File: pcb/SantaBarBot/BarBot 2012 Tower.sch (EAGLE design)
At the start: 42 parts, among them J1 AVR_SPI_PRG_62X3_LOCK, U1 ATMEGA328P, U2 L298_BRIDGE_DRIVER, U3 742G04DBVR, U5 LMV324IDR, U6 SN75HVD179D, U7 742G04DBVR, U8 SN75HVD179D, U9 LMV324IDR

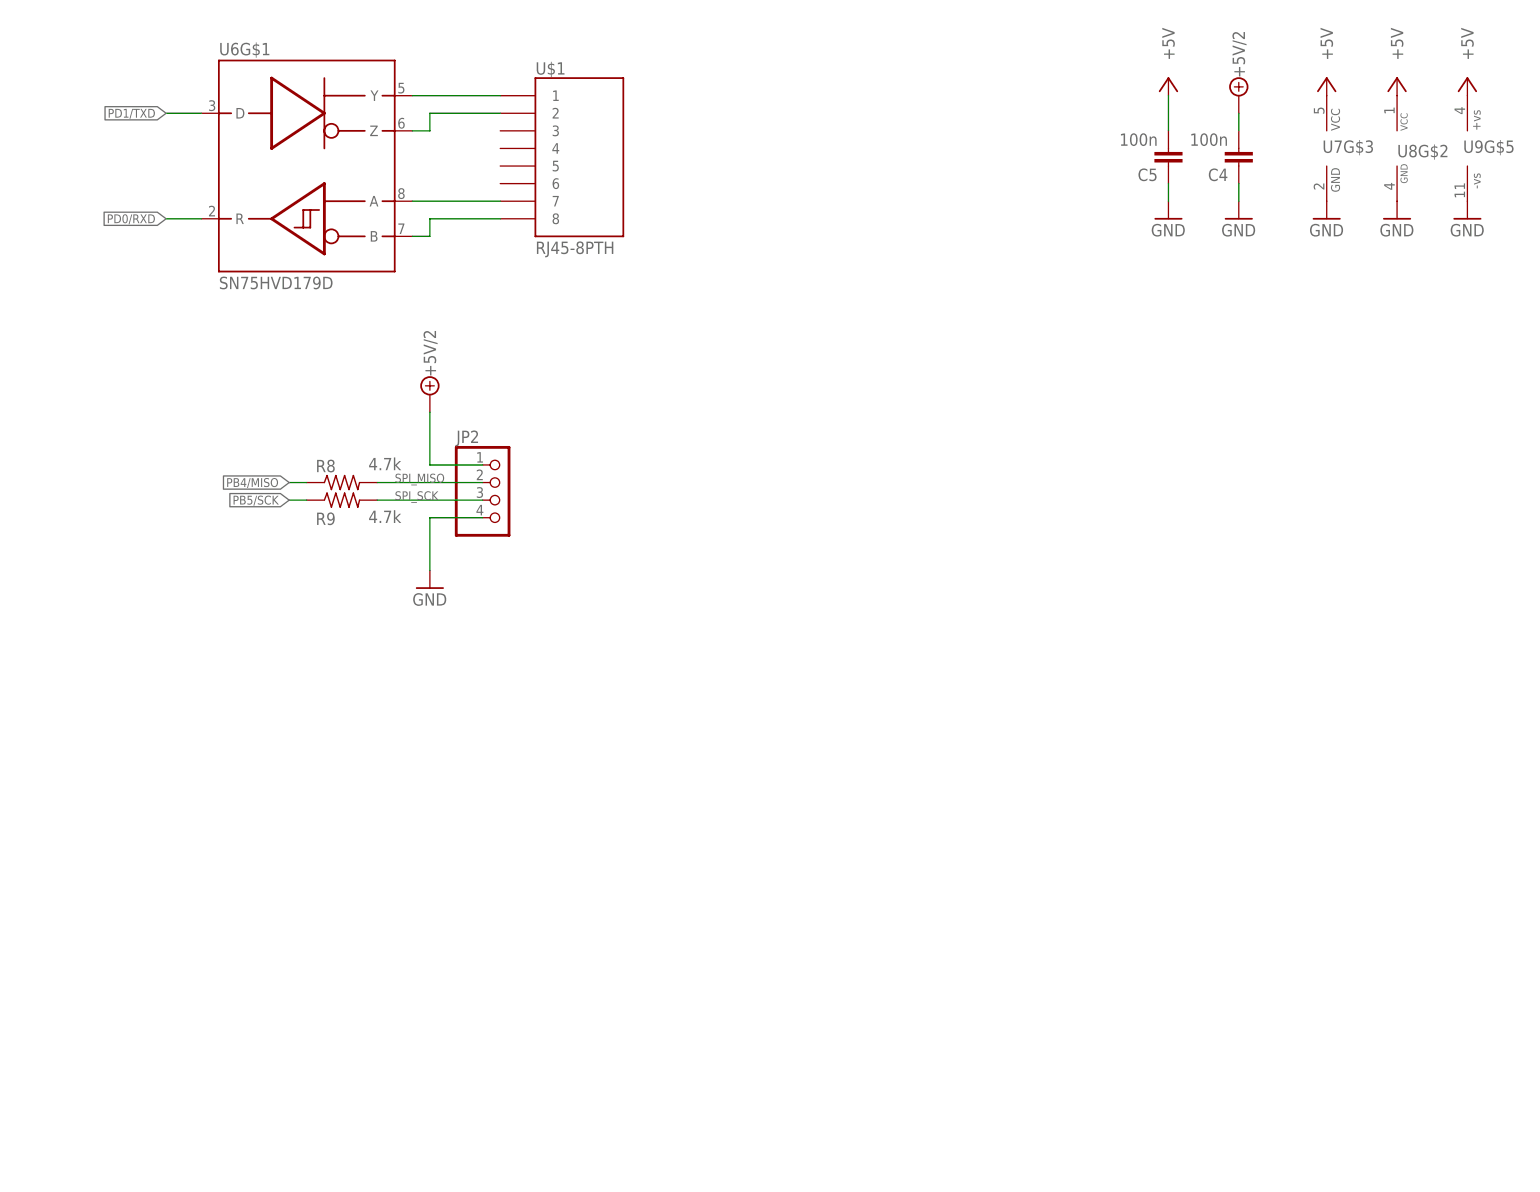
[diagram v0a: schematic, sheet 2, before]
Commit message: Started PCB layout, cleaning up schematic.  Added RS485 termination, fixed duplicate chips
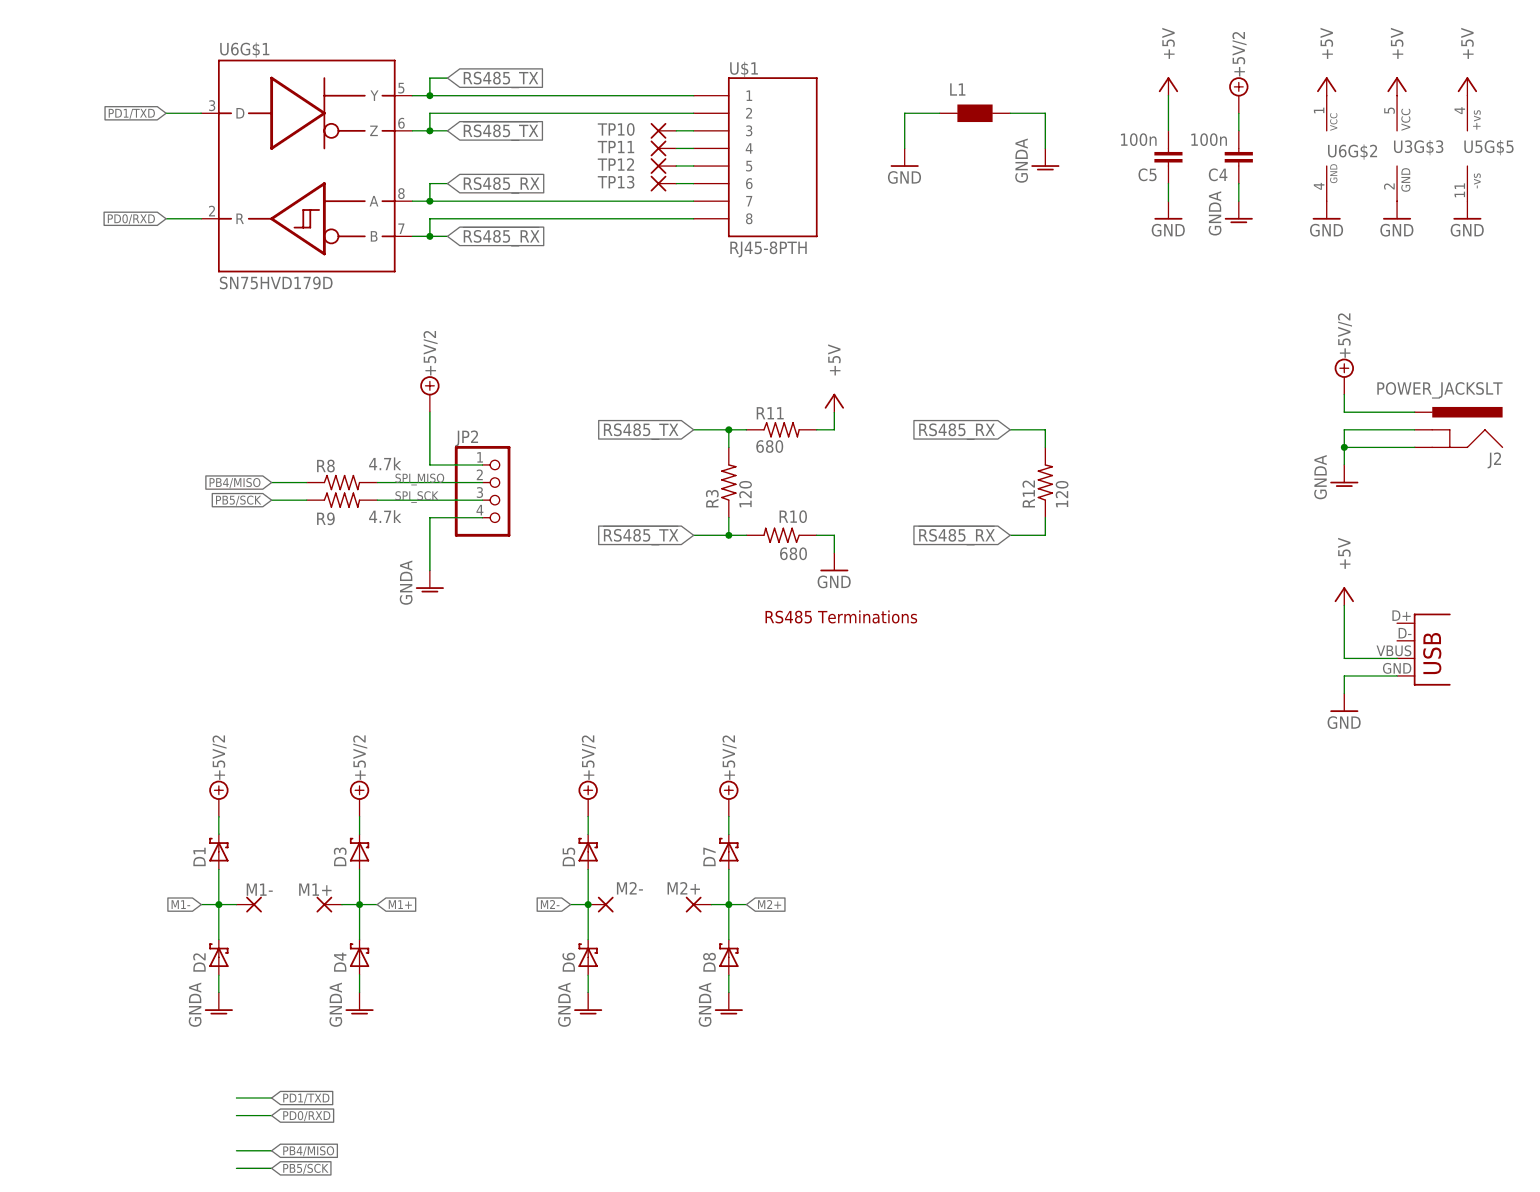
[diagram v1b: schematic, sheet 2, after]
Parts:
- removed TP1, TP2, TP3, TP4, TP5, TP6, TP7, TP8, TP9: (no value), wirepad:1,6/0,8
- removed U7: 742G04DBVR, 74xx-little-us:742G04DBVR
- removed U8: SN75HVD179D, texas:SN75HVD179D
- removed U9: LMV324IDR, bb_parts_OpAmp:LMV324IDR
- added D1, D2, D3, D4, D5, D6, D7, D8: (no value), diode:SCHOTTKY-DIODESMD
- added J2: POWER_JACKSLT, SparkFun-Connectors:POWER_JACKSLT
- added JP1: USB-B, SparkFun-Connectors:USBPTH
- added L1: (no value), wuerth-elektronik:WE-CBF_0805
- added R10, R11: 680, rcl:R-US_R2012
- added R12, R3: 120, rcl:R-US_R2012
- added TP10, TP11, TP12, TP13: (no value), wirepad:1,6/0,8
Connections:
- removed net N$11: U$1.8, U6G$1.B
- removed net N$12: U$1.7, U6G$1.A
- removed net N$13: U$1.2, U6G$1.Z
- removed net N$14: U$1.1, U6G$1.Y
- removed net N$6: M2-.P, U2.OUT3
- new net !RS485_RX: R12.1, U$1.8, U6G$1.B
- new net !RS485_TX: R10.2, R3.1, U$1.2, U6G$1.Z
- new net GNDA: C4.1, D2.A, D4.A, D6.A, D8.A, J2.GND, J2.GNDBREAK, JP2.4, L1.2, R4.1, R5.1
- new net M1+: D3.A, D4.C, M1+.P, U2.OUT1
- new net M1-: D1.A, D2.C, M1-.P, U2.OUT2
- new net M2+: D7.A, D8.C, M2+.P, U2.OUT4
- new net M2-: D5.A, D6.C, M2-.P, U2.OUT3
- new net N$1: TP10.P, U$1.3
- new net RS485_RX: R12.2, U$1.7, U6G$1.A
- new net RS485_TX: R11.1, R3.2, U$1.1, U6G$1.Y
- net !PD4/XCK/T0: no longer TP6.P
- net !PD7/AIN1: no longer TP7.P
- net +5V: now also JP1.VBUS, R11.2, U3G$3.VCC, U5G$5.+VS, U6G$2.VCC; no longer U7G$3.VCC, U8G$2.VCC, U9G$5.+VS
- net +5V/2: now also D1.C, D3.C, D5.C, D7.C, J2.PWR
- net AREF: no longer TP1.P
- net GND: now also JP1.GND, L1.1, R10.1, U3G$3.GND, U5G$5.-VS, U6G$2.GND; no longer C4.1, JP2.4, R4.1, R5.1, U7G$3.GND, U8G$2.GND, U9G$5.-VS
- net N$2: now also TP11.P, U$1.4; no longer M1+.P, U2.OUT1
- net N$4: now also TP12.P, U$1.5; no longer M1-.P, U2.OUT2
- net N$5: now also TP13.P, U$1.6; no longer M2+.P, U2.OUT4
- net PC0/ADC0: no longer TP3.P
- net PC1/ADC1: no longer TP2.P
- net PD4/XCK/T0: no longer TP4.P
- net PD5/T1: no longer TP8.P
- net PD6/AIN0: no longer TP9.P
- net PD7/AIN1: no longer TP5.P
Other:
- note added: "RS485 Terminations"
- moved on the sheet: U$1

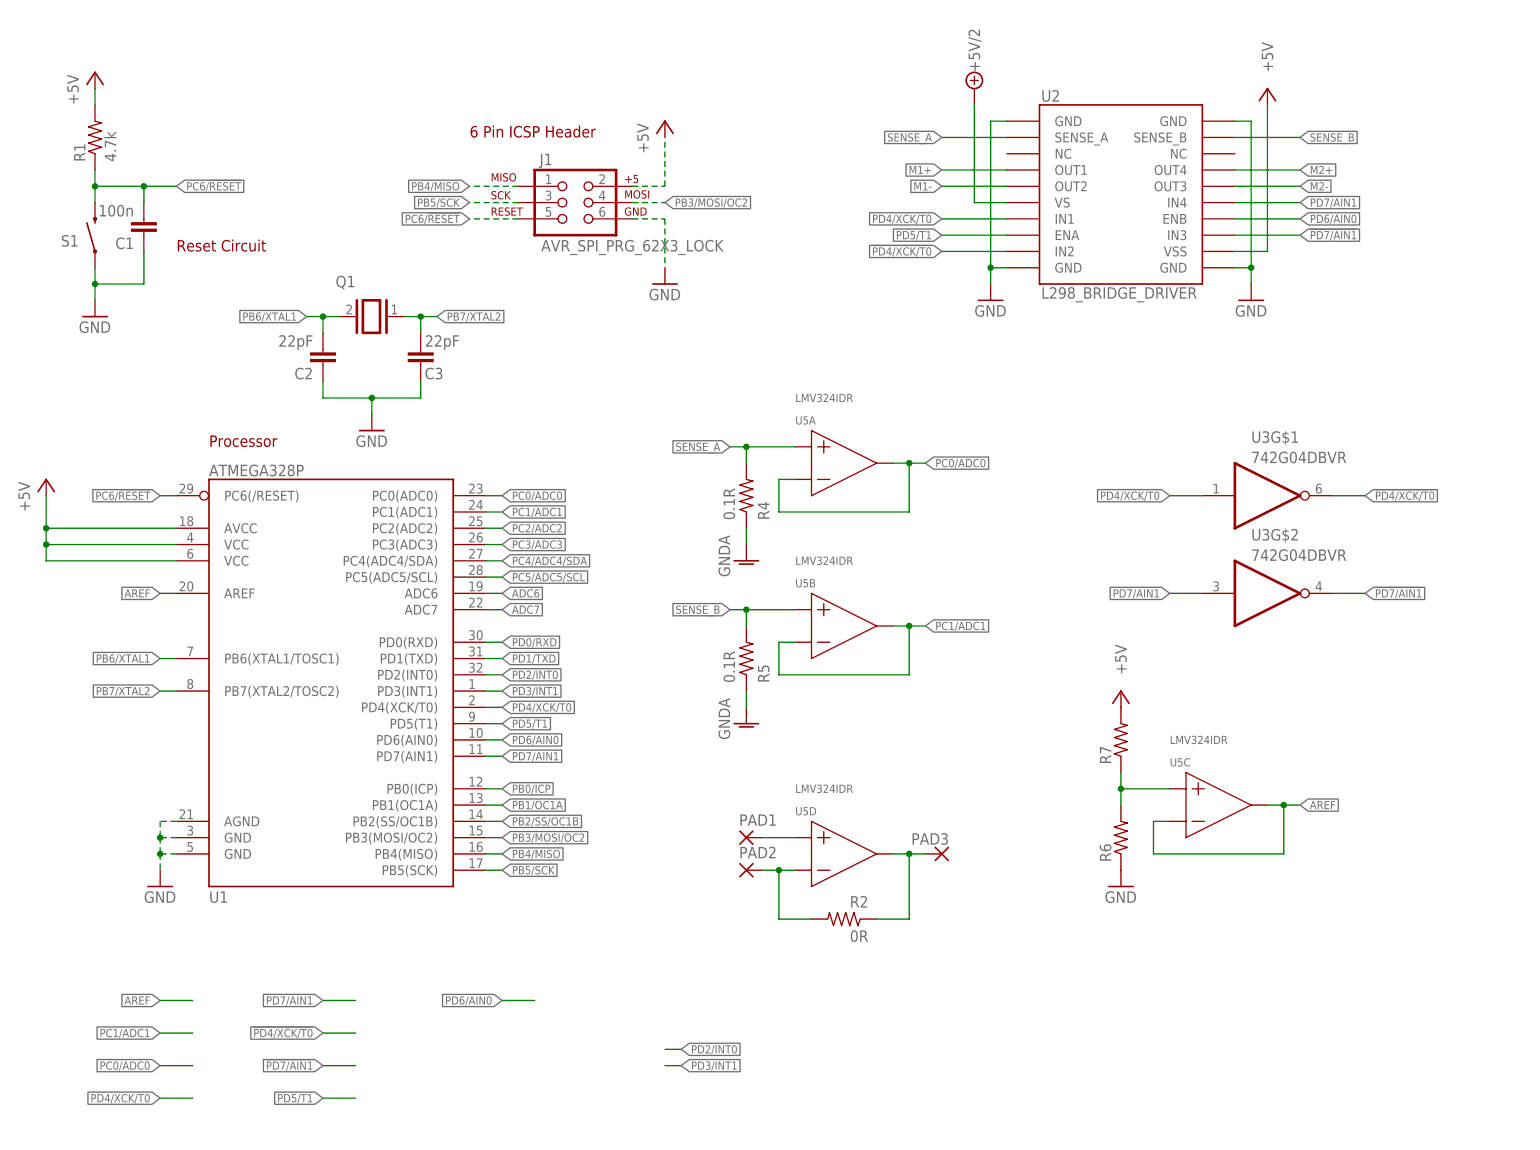
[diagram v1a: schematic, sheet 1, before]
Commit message: Finished routing PCB, added PDFs of board and schematic to directory, generated netlist, pinlist, and partslist for design
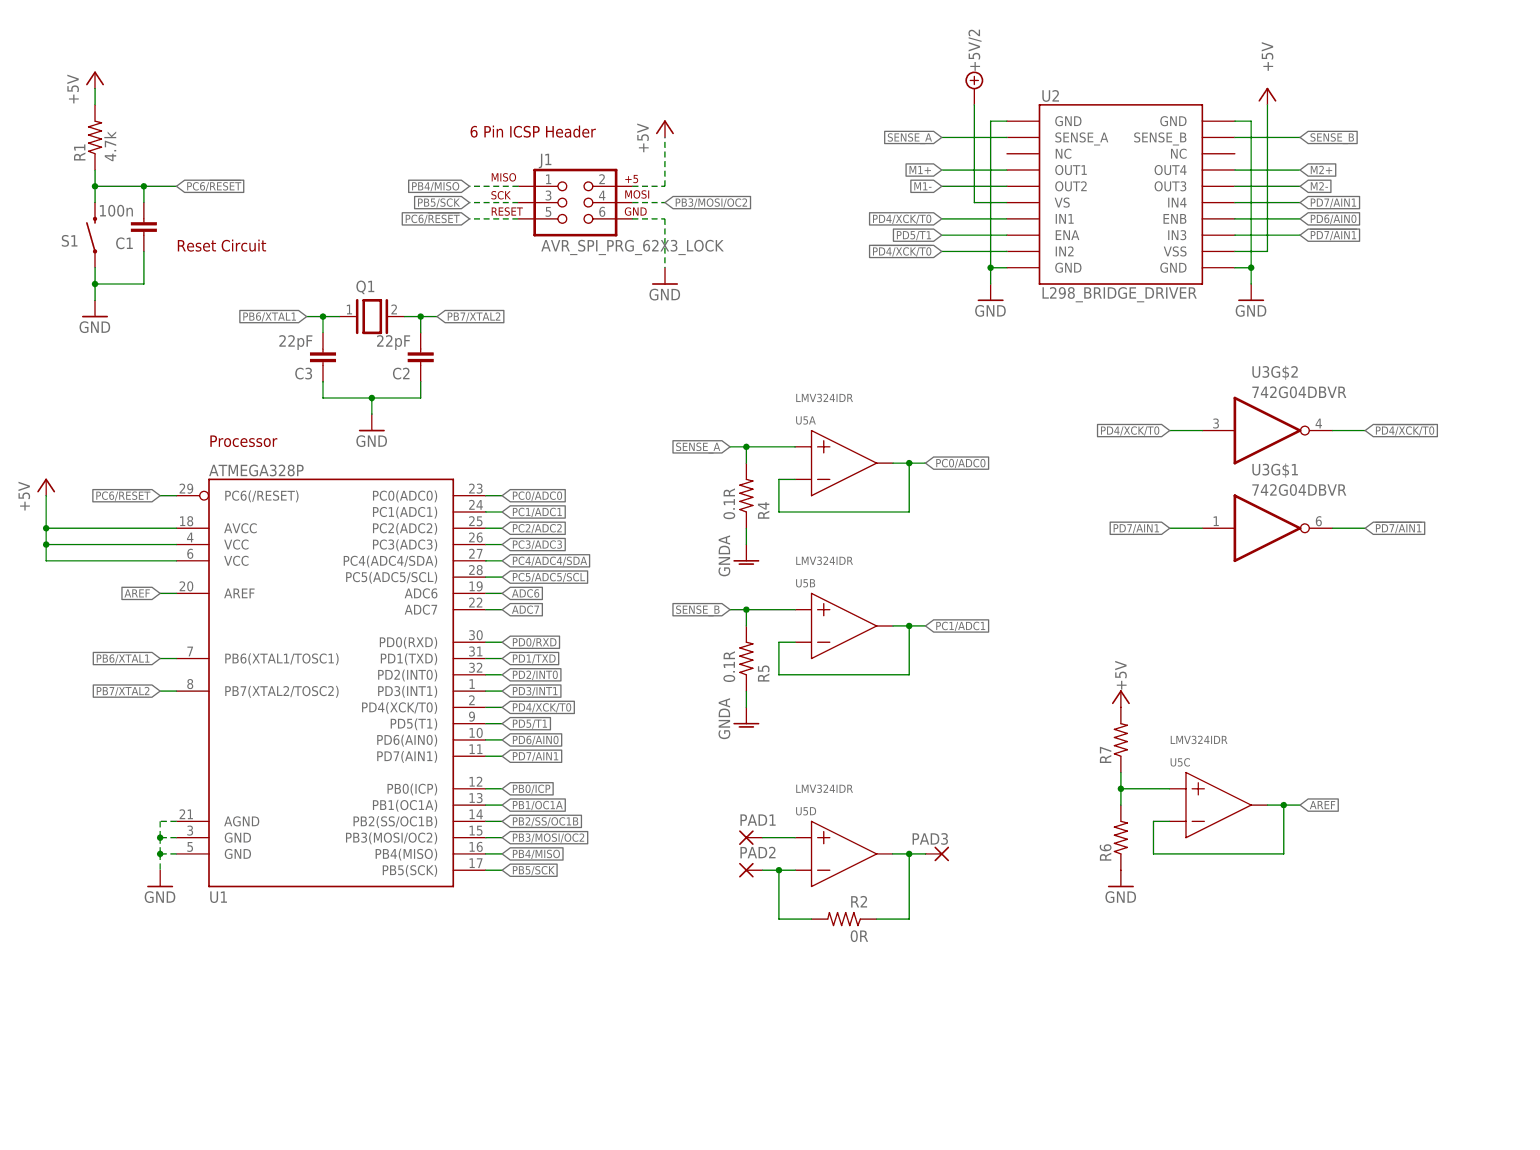
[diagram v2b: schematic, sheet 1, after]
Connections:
- net !PD4/XCK/T0: now also U3G$2.O; no longer U3G$1.O
- net !PD7/AIN1: now also U3G$1.O; no longer U3G$2.O
- net PB6/XTAL1: now also C3.2, Q1.1; no longer C2.2, Q1.2
- net PB7/XTAL2: now also C2.2, Q1.2; no longer C3.2, Q1.1
- net PD4/XCK/T0: now also U3G$2.I; no longer U3G$1.I
- net PD7/AIN1: now also U3G$1.I; no longer U3G$2.I
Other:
- moved on the sheet: C2, C3, Q1, U3G$1, U3G$2
